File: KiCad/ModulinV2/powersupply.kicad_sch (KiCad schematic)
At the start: 31 parts, among them IC27 L7812CD2T-TR, IC28 L7912CD2T-TR, IC29 NCP5500DADJR2G, IC30 NCP5500DADJR2G, J2 PJ-002B

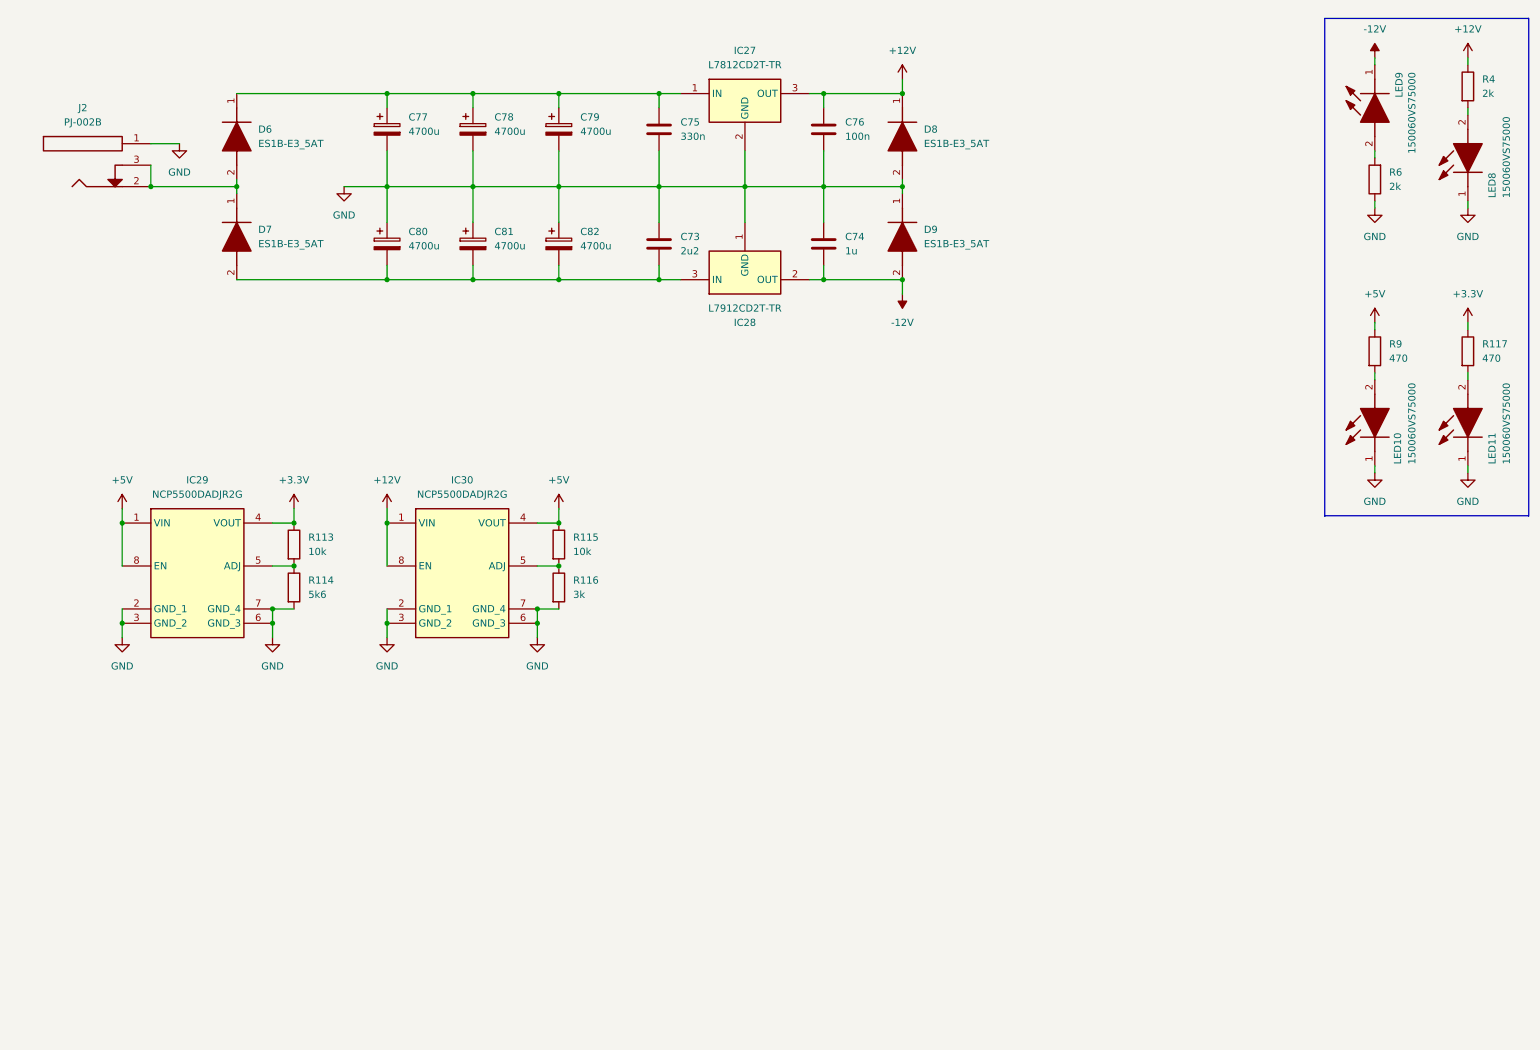
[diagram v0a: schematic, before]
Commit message: Designed ADSR and better tuning schematics with digital/manual capability
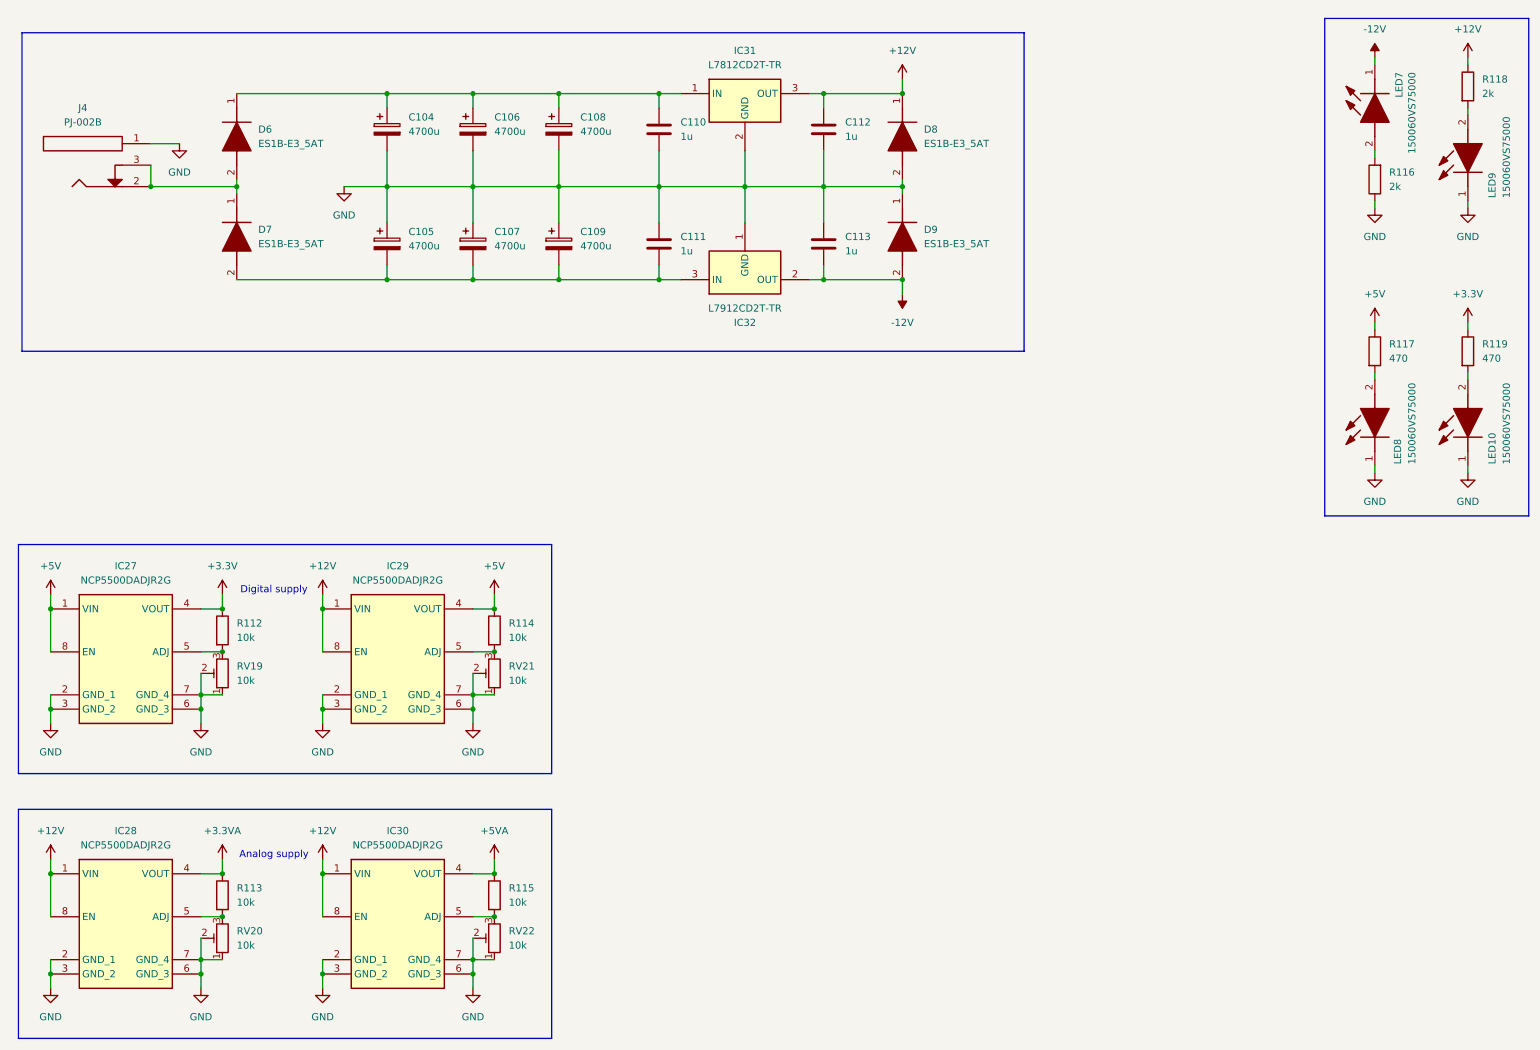
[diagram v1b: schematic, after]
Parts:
- removed R114: 5k6, symbol Device:R
- removed R116: 3k, symbol Device:R
- added IC28, IC30: NCP5500DADJR2G, SOIC127P600X175-8N, symbol NCP5500DADJR2G:NCP5500DADJR2G
- added R113, R115: 10k, symbol Device:R
- added RV19, RV20, RV21, RV22: 10k, symbol Device:R_Potentiometer_Trim
- C110: renamed from C75; value 330n -> 1u
- C111: renamed from C73; value 2u2 -> 1u
- C112: renamed from C76; value 100n -> 1u
- renumbered C77 to C104, C80 to C105, C78 to C106, C81 to C107, C79 to C108, C82 to C109, C74 to C113, IC29 to IC27, IC30 to IC29, IC27 to IC31, IC28 to IC32, J2 to J4, LED11 to LED10, LED9 to LED7, LED10 to LED8, LED8 to LED9, R113 to R112, R115 to R114, R6 to R116, R9 to R117, R4 to R118, R117 to R119
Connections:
- net +12V: now also IC28.1 (VIN), IC28.8 (EN), IC30.1 (VIN), IC30.8 (EN)
- net GND: now also IC28.2 (GND_1), IC28.3 (GND_2), IC28.6 (GND_3), IC28.7 (GND_4), IC30.2 (GND_1), IC30.3 (GND_2), IC30.6 (GND_3), IC30.7 (GND_4), RV19.1, RV19.2, RV20.1, RV20.2, RV21.1, RV21.2, RV22.1, RV22.2
- net at IC29.5 (ADJ), R114.2: now also RV21.3
- net at IC27.5 (ADJ), R112.2: now also RV19.3
- new net: IC30.5 (ADJ), R115.2, RV22.3
- new net: IC28.5 (ADJ), R113.2, RV20.3
- new net +3.3VA: IC28.4 (VOUT), R113.1
- new net +5VA: IC30.4 (VOUT), R115.1
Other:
- note added: "Analog supply"
- note added: "Digital supply"
- moved on the sheet: IC27, IC29, R112, R114

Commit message: Added 4k7 pullups to I2C lines
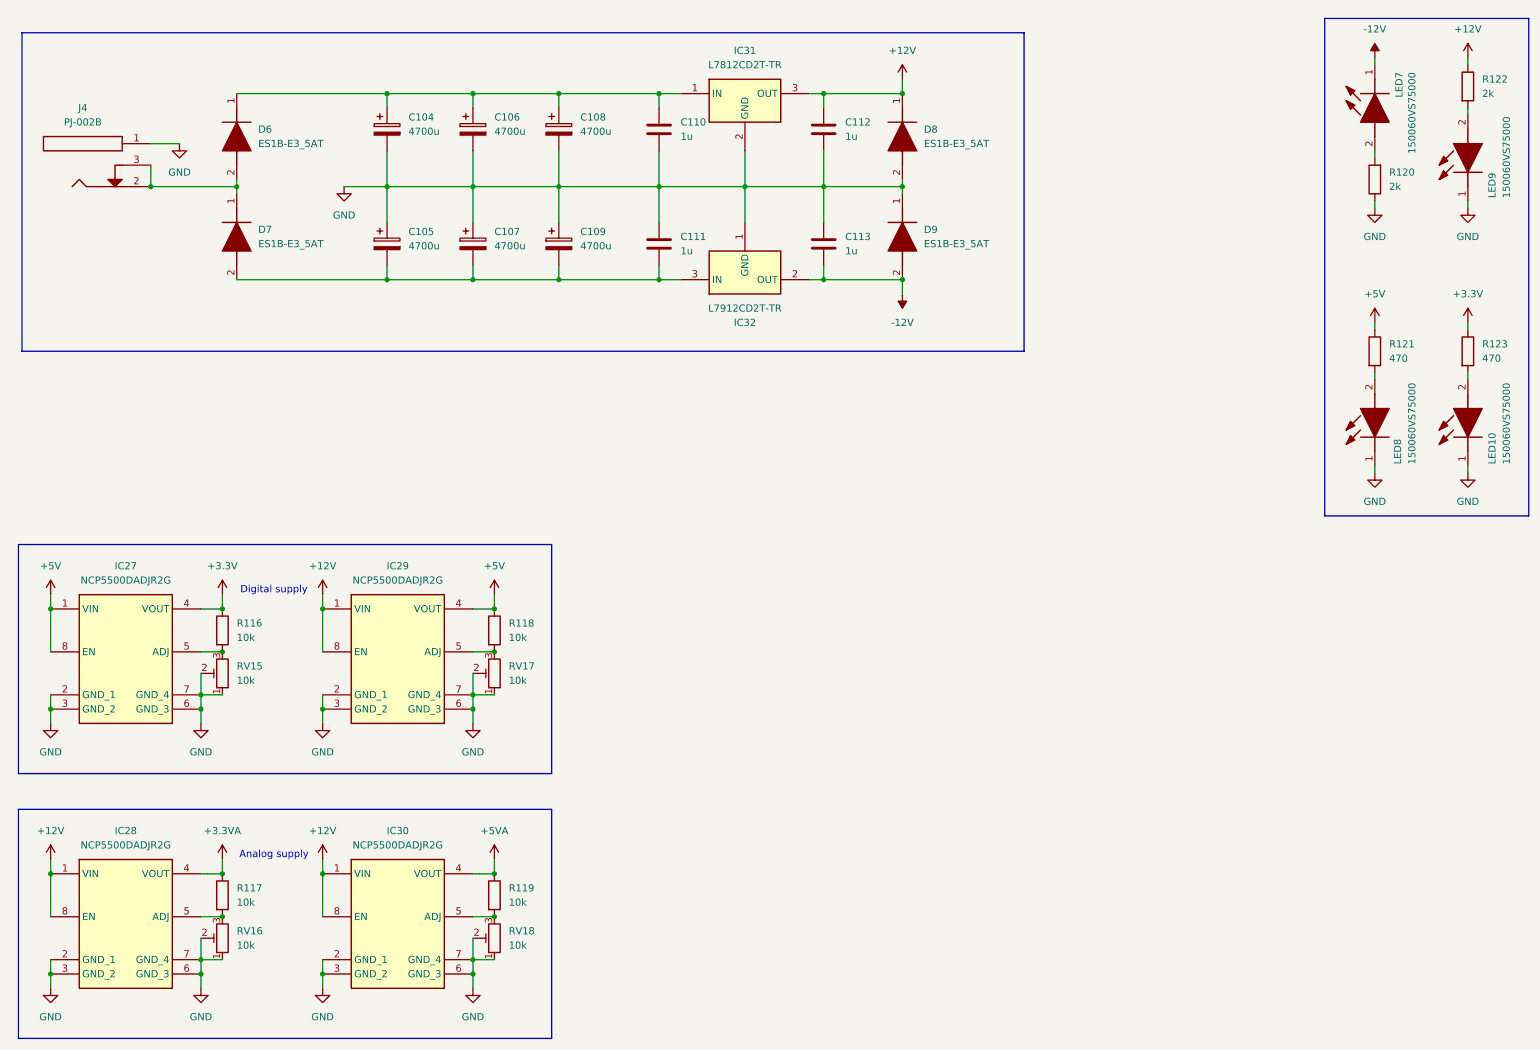
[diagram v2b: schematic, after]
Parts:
- renumbered R112 to R116, R113 to R117, R114 to R118, R115 to R119, R116 to R120, R117 to R121, R118 to R122, R119 to R123, RV19 to RV15, RV20 to RV16, RV21 to RV17, RV22 to RV18

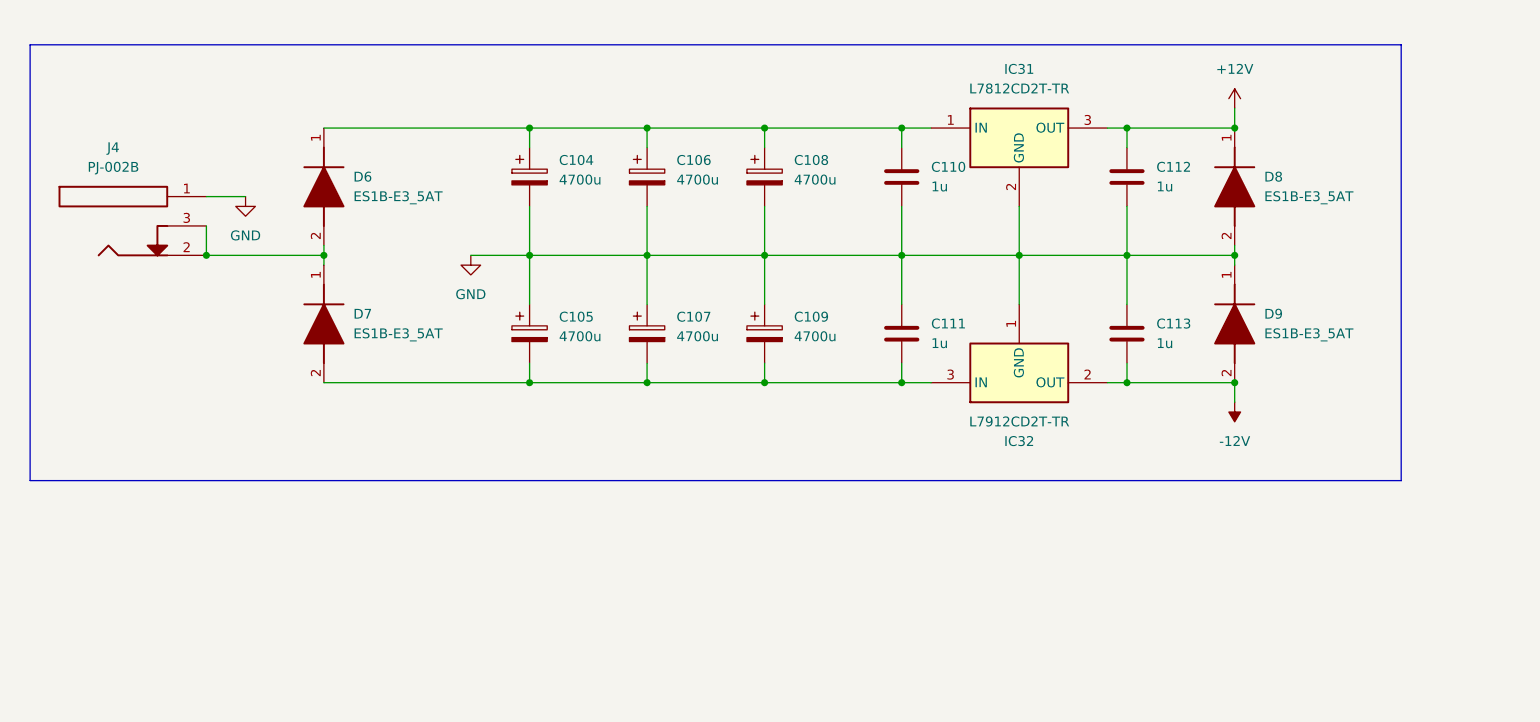
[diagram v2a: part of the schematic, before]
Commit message: Modified supply schematic and made modulation wheel initial design
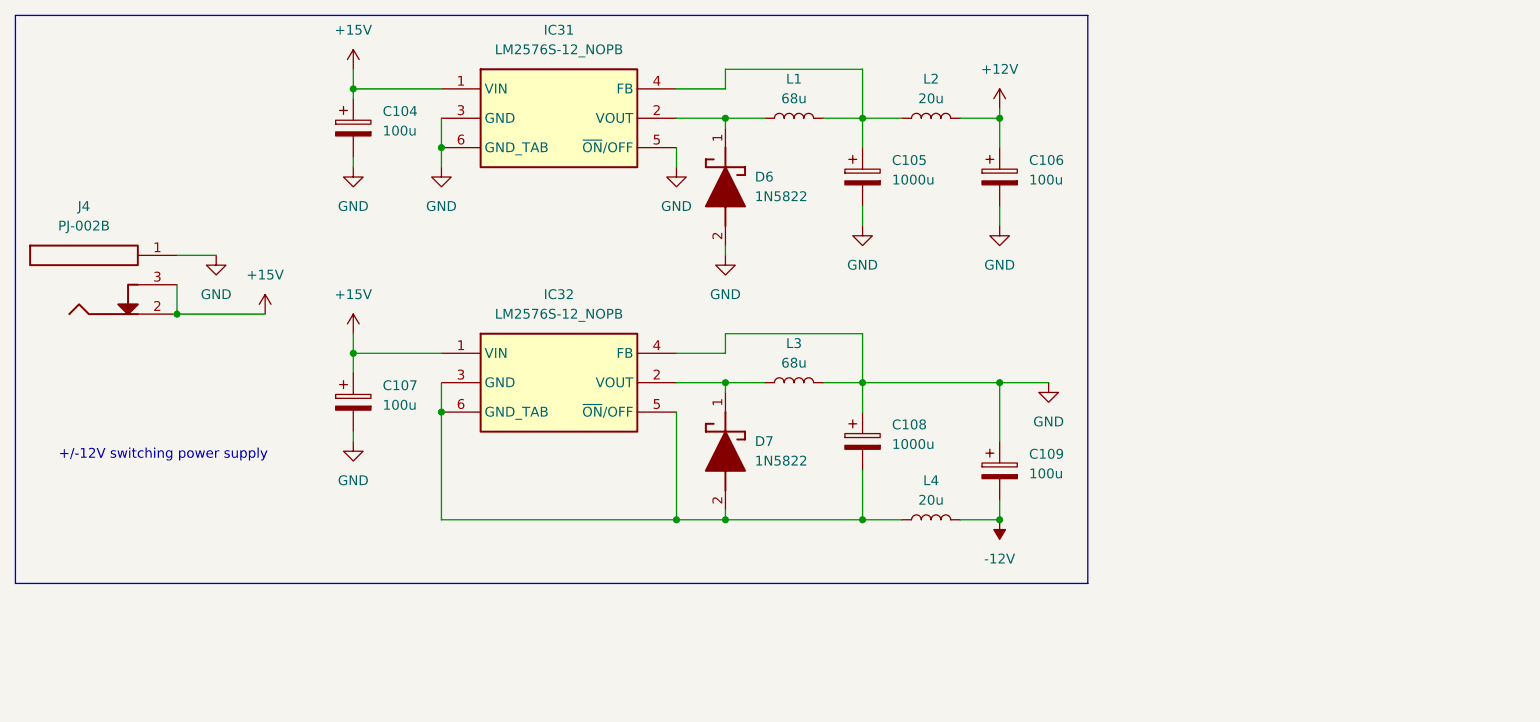
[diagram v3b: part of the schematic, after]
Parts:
- removed C110, C111, C112, C113: 1u, symbol Device:C
- removed D6, D7, D8, D9: ES1B-E3_5AT, DIOM5127X229N, symbol ES1B-E3_5AT:ES1B-E3_5AT
- removed IC31: L7812CD2T-TR, L7812CD2TTR, symbol L7812CD2T-TR:L7812CD2T-TR
- removed IC32: L7912CD2T-TR, L7905CD2TTR, symbol L7912CD2T-TR:L7912CD2T-TR
- added D6, D7: 1N5822, DIOAD3070W130L950D530, symbol 1N5822:1N5822
- added IC31, IC32: LM2576S-12_NOPB, TO170P1435X465-6N, symbol LM2576S-12_NOPB:LM2576S-12_NOPB
- added L1, L3: 68u, symbol Device:L
- added L2, L4: 20u, symbol Device:L
- C104, C106, C107, C109: value 4700u -> 100u
- C105, C108: value 4700u -> 1000u
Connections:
- net +12V: now also C106.1, L2.2
- net -12V: now also C109.2, L4.2
- net GND: now also C105.2, C107.2, C108.1, D6.2 (A), IC31.3 (GND), IC31.5 (~{ON}/OFF), IC31.6 (GND_TAB), IC32.4 (FB), L3.2; no longer C105.1, C107.1, C108.2
- net +15V: now reaches J4.2, J4.3
- net +15V: now also C104.1, C107.1, IC31.1 (VIN), IC32.1 (VIN)
- new net: D7.1 (K), IC32.2 (VOUT), L3.1
- new net: C108.2, D7.2 (A), IC32.3 (GND), IC32.5 (~{ON}/OFF), IC32.6 (GND_TAB), L4.1
- new net: C105.1, IC31.4 (FB), L1.2, L2.1
- new net: D6.1 (K), IC31.2 (VOUT), L1.1
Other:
- note added: "+/-12V switching power supply"
- moved on the sheet: J4
